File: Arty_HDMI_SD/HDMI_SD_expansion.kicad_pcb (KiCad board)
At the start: 2 copper layers, 13 parts, among them J1 0015912120, J2 SD_card_slot, J3 0015912120, J4 2000-1-2-41-00-BK

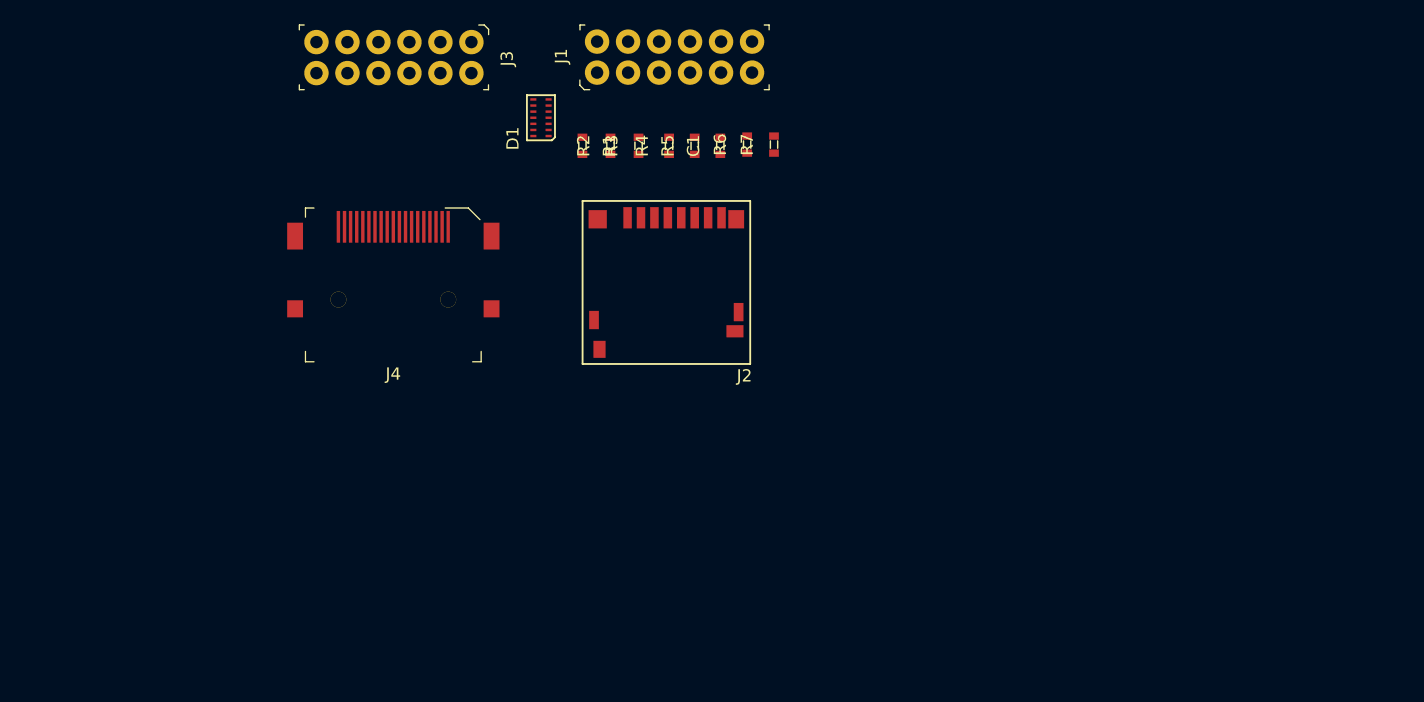
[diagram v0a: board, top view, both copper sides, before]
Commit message: Added USB SPI Interface
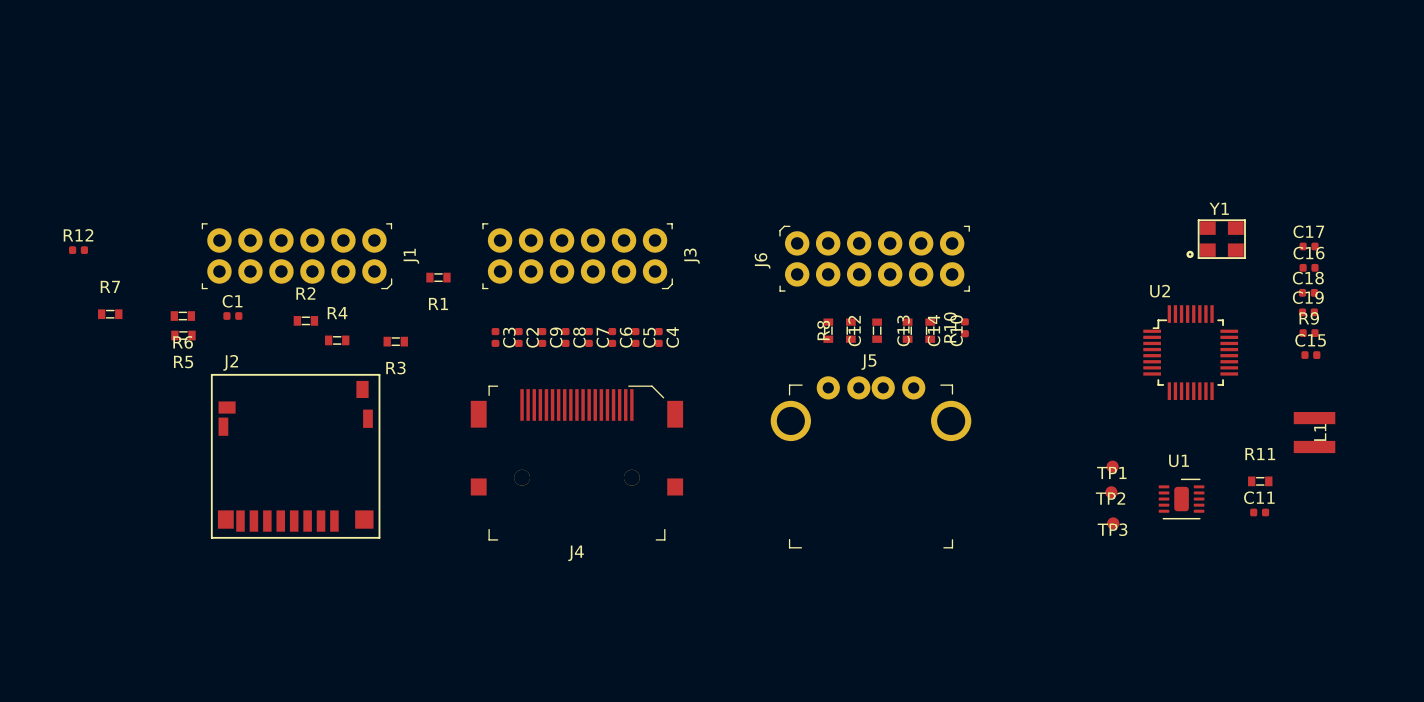
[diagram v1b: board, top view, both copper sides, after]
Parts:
- removed D1: TPD6E05U06, antmicro-footprints:TPD6E05U06
- added C10: C_22u_0603, antmicro-footprints:0603-cap, F.Cu at (164.2, 96.2)
- added C11: C_10n_0402, antmicro-footprints:0402-cap, F.Cu at (191.2, 111.0)
- added C12: C_22u_0603, antmicro-footprints:0603-cap, F.Cu at (155.8, 96.2)
- added C13: C_22u_0603, antmicro-footprints:0603-cap, F.Cu at (159.8, 96.2)
- added C14: C_22u_0603, antmicro-footprints:0603-cap, F.Cu at (162.3, 96.2)
- added C15: C_100n_0402_6V3, antmicro-footprints:0402-cap, F.Cu at (195.4, 98.2)
- added C16: C_22p_0402, antmicro-footprints:0402-cap, F.Cu at (195.2, 91.0)
- added C17: C_22p_0402, antmicro-footprints:0402-cap, F.Cu at (195.2, 89.2)
- added C18: C_100n_0402_6V3, antmicro-footprints:0402-cap, F.Cu at (195.2, 93.0)
- added C19: C_100n_0402_6V3, antmicro-footprints:0402-cap, F.Cu at (195.2, 94.7)
- added C2: C_100n_0402_6V3, antmicro-footprints:0402-cap, F.Cu at (130.5, 96.7)
- added C3: C_100n_0402_6V3, antmicro-footprints:0402-cap, F.Cu at (128.6, 96.7)
- added C4: C_100n_0402_6V3, antmicro-footprints:0402-cap, F.Cu at (142.0, 96.7)
- added C5: C_100n_0402_6V3, antmicro-footprints:0402-cap, F.Cu at (140.1, 96.7)
- added C6: C_100n_0402_6V3, antmicro-footprints:0402-cap, F.Cu at (138.1, 96.7)
- added C7: C_100n_0402_6V3, antmicro-footprints:0402-cap, F.Cu at (136.2, 96.7)
- added C8: C_100n_0402_6V3, antmicro-footprints:0402-cap, F.Cu at (134.3, 96.7)
- added C9: C_100n_0402_6V3, antmicro-footprints:0402-cap, F.Cu at (132.4, 96.7)
- added J5: UE27AC54100, antmicro-footprints:USB_A_Female_UE27AC54100, F.Cu at (159.3, 103.5)
- added J6: 0015912120, antmicro-footprints:PinHeader_6x2_P2.54mm_Horizontal_Mirrored, F.Cu at (153.3, 88.8)
- added L1: XFL4020-102MEB, antmicro-footprints:XFL4020-102MEB, F.Cu at (195.7, 104.5)
- added R10: R_22R_0402, antmicro-footprints:0402-res, F.Cu at (167.1, 95.9)
- added R11: R_0R_0603, antmicro-footprints:0603-res, F.Cu at (191.2, 108.5)
- added R12: R_220R_0402, antmicro-footprints:0402-res, F.Cu at (94.4, 89.5)
- added R8: R_0R_0603, antmicro-footprints:0603-res, F.Cu at (157.7, 96.2)
- added R9: R_22R_0402, antmicro-footprints:0402-res, F.Cu at (195.2, 96.3)
- added TP1: TP_SMD1MM, antmicro-footprints:Testpoint_smd_1mm, F.Cu at (179.2, 107.3)
- added TP2: TP_SMD1MM, antmicro-footprints:Testpoint_smd_1mm, F.Cu at (179.1, 109.5)
- added TP3: TP_SMD1MM, antmicro-footprints:Testpoint_smd_1mm, F.Cu at (179.2, 112.0)
- added U1: TPS61232DRCT, antmicro-footprints:VSON-10-1EP_3x3mm, F.Cu at (184.6, 110.2)
- added U2: MAX3421EEHJ, antmicro-footprints:TQFP-32_5x5mm, F.Cu at (185.6, 98.0)
- added Y1: KX-7_12,MHz, antmicro-footprints:KX-7, F.Cu at (188.1, 88.6)
- C1: value C_1u_0603 -> C_100n_0402_6V3; footprint antmicro-footprints:0603-cap -> antmicro-footprints:0402-cap
- J1, J3: footprint antmicro-footprints:PinHeader_6x2_P2.54mm_Horizontal -> antmicro-footprints:PinHeader_6x2_P2.54mm_Horizontal_Mirrored
- J2: value SD_card_slot -> 1140084168; footprint antmicro-footprints:1140084168 -> antmicro-footprints:MicroSD_1140084168
- R1, R2, R3, R4, R5, R6, R7: value R_10k_0603 -> R_20k_0603
- moved R7 56.1 mm to (97.0, 94.8), turned to 0 degrees
- moved R6 48.3 mm to (103.0, 95.0), turned to 180 degrees
- moved R5 44.7 mm to (103.0, 96.5), turned to 180 degrees
- moved C1 42.3 mm to (107.0, 95.0), turned to 0 degrees
- moved J2 40.0 mm to (112.2, 106.5), turned to 0 degrees
- moved R4 31.5 mm to (115.6, 97.0), turned to 0 degrees
- moved R2 28.8 mm to (113.0, 95.3), turned to 0 degrees
- moved R3 25.6 mm to (120.4, 97.0), turned to 180 degrees
- moved J1 24.6 mm to (118.7, 91.5), turned to 270 degrees
- moved J3 24.2 mm to (141.7, 91.5)
- moved J4 21.0 mm to (135.2, 106.7)
- moved R1 16.0 mm to (123.9, 91.8), turned to 180 degrees
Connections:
- J1 pad 1: /SS -> /CD_DAT3
- J1 pad 11: +5V -> +3V3
- J1 pad 12: +5V -> +3V3
- J1 pad 2: /MOSI -> /DAT1
- J1 pad 3: /MOSI -> /MOSI_CMD
- J1 pad 4: /SCK -> /DAT2
- J1 pad 5: /MISO -> /MISO_DAT0
- J1 pad 6: /TDMS_D1_P -> /CD
- J1 pad 8: /TDMS_D1_N -> /NC_EN
- J2 pad 10: /CD2 -> GND
- J2 pad 2: /SS -> /CD_DAT3
- J2 pad 3: /MOSI -> /MOSI_CMD
- J2 pad 7: /MISO -> /MISO_DAT0
- J2 pad 9: /CD -> Net-(J2-Pad9)
- J2 pad ~: (no net) -> GND
- J3 pad 11: +5V -> +3V3
- J3 pad 12: +5V -> +3V3
- J4 pad 1: /TDMS_D2_P -> /C_TDMS_D2_P
- J4 pad 10: /TDMS_CLK_N -> /C_TDMS_CLK_P
- J4 pad 12: /TDMS_CLK_P -> /C_TDMS_CLK_N
- J4 pad 18: +5V -> /NC
- J4 pad 3: /TDMS_D2_N -> /C_TDMS_D2_N
- J4 pad 4: /TDMS_D1_P -> /C_TDMS_D1_P
- J4 pad 6: /TDMS_D1_N -> /C_TDMS_D1_N
- J4 pad 7: /TDMS_D0_P -> /C_TDMS_D0_P
- J4 pad 9: /TDMS_D0_N -> /C_TDMS_D0_N
- R1 pad 2: /DAT2 -> /CD
- R2 pad 2: /SS -> /DAT1
- R3 pad 2: /MOSI -> /MISO_DAT0
- R5 pad 2: /MISO -> /MOSI_CMD
- R6 pad 2: /DAT1 -> /CD_DAT3
- R7 pad 2: /CD -> /DAT2

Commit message: Schematic updates
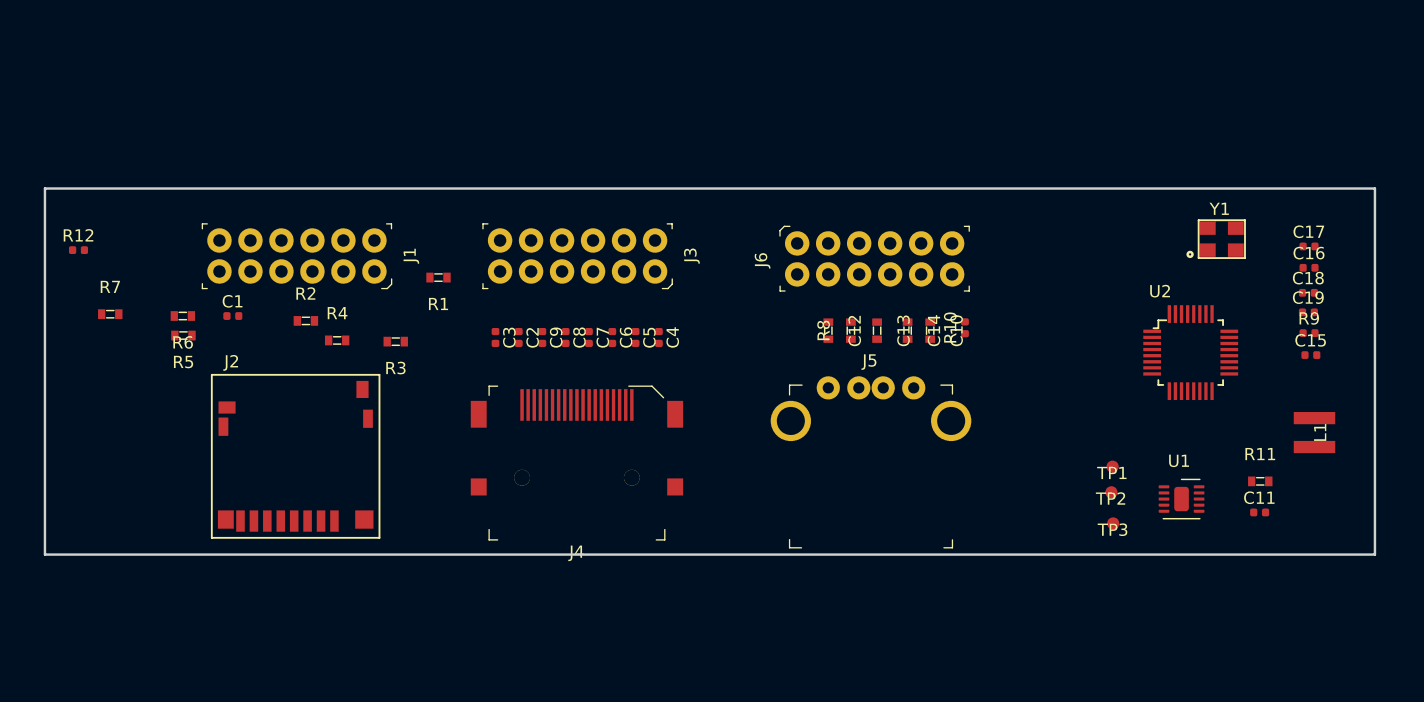
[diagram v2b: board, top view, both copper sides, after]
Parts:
- R11: value R_0R_0603 -> R_10k_0603
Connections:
- J5 pad 1: GND -> Net-(C15-Pad1)
- J5 pad 2: Net-(D1-Pad2) -> Net-(J5-Pad2)
- J5 pad 3: Net-(J5-Pad3) -> Net-(D1-Pad2)
- J5 pad 4: Net-(C15-Pad1) -> GND
- J5 pad SH: GND -> Net-(J5-PadSH)
- J6 pad 2: Net-(J6-Pad2) -> /GPX_USB
- J6 pad 4: Net-(J6-Pad4) -> /RST_USB
- R9 pad 1: Net-(J5-Pad3) -> Net-(J5-Pad2)
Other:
- board outline added: 109 x 30 mm

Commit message: Added testpads
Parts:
- added TP10: TP_SMD1MM, antmicro-footprints:Testpoint_smd_1mm, F.Cu at (173.9, 112.5)
- added TP4: TP_SMD1MM, antmicro-footprints:Testpoint_smd_1mm, F.Cu at (179.0, 105.0)
- added TP5: TP_SMD1MM, antmicro-footprints:Testpoint_smd_1mm, F.Cu at (183.0, 104.2)
- added TP6: TP_SMD1MM, antmicro-footprints:Testpoint_smd_1mm, F.Cu at (185.9, 104.1)
- added TP7: TP_SMD1MM, antmicro-footprints:Testpoint_smd_1mm, F.Cu at (179.4, 101.6)
- added TP8: TP_SMD1MM, antmicro-footprints:Testpoint_smd_1mm, F.Cu at (173.8, 110.5)
- added TP9: TP_SMD1MM, antmicro-footprints:Testpoint_smd_1mm, F.Cu at (173.7, 104.5)
- moved J6 11.6 mm to (164.7, 91.3), turned to 270 degrees
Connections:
- J6 pad 6: Net-(J6-Pad6) -> /INT_USB
- R11 pad 2: Net-(R11-Pad2) -> /INT_USB
- U2 pad 18: Net-(R11-Pad2) -> /INT_USB

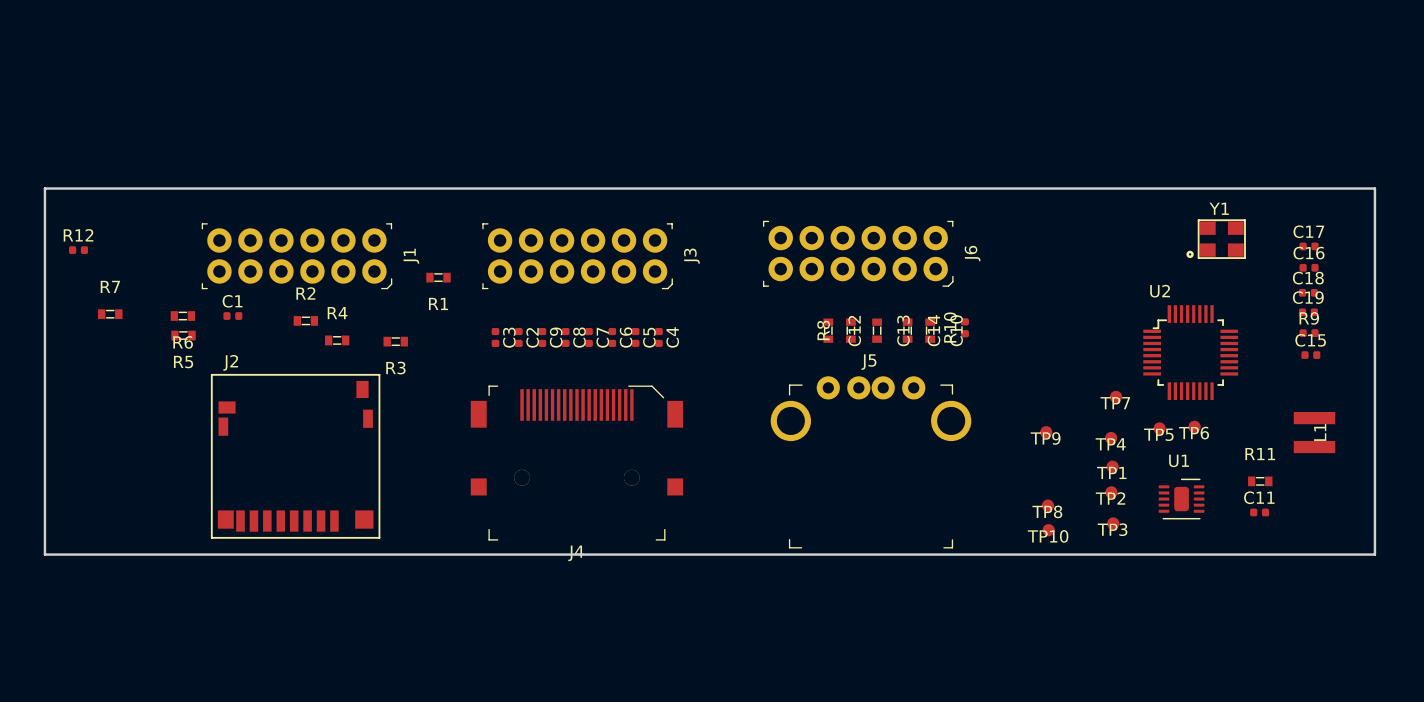
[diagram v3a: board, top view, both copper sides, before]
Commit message: Optimized component placement
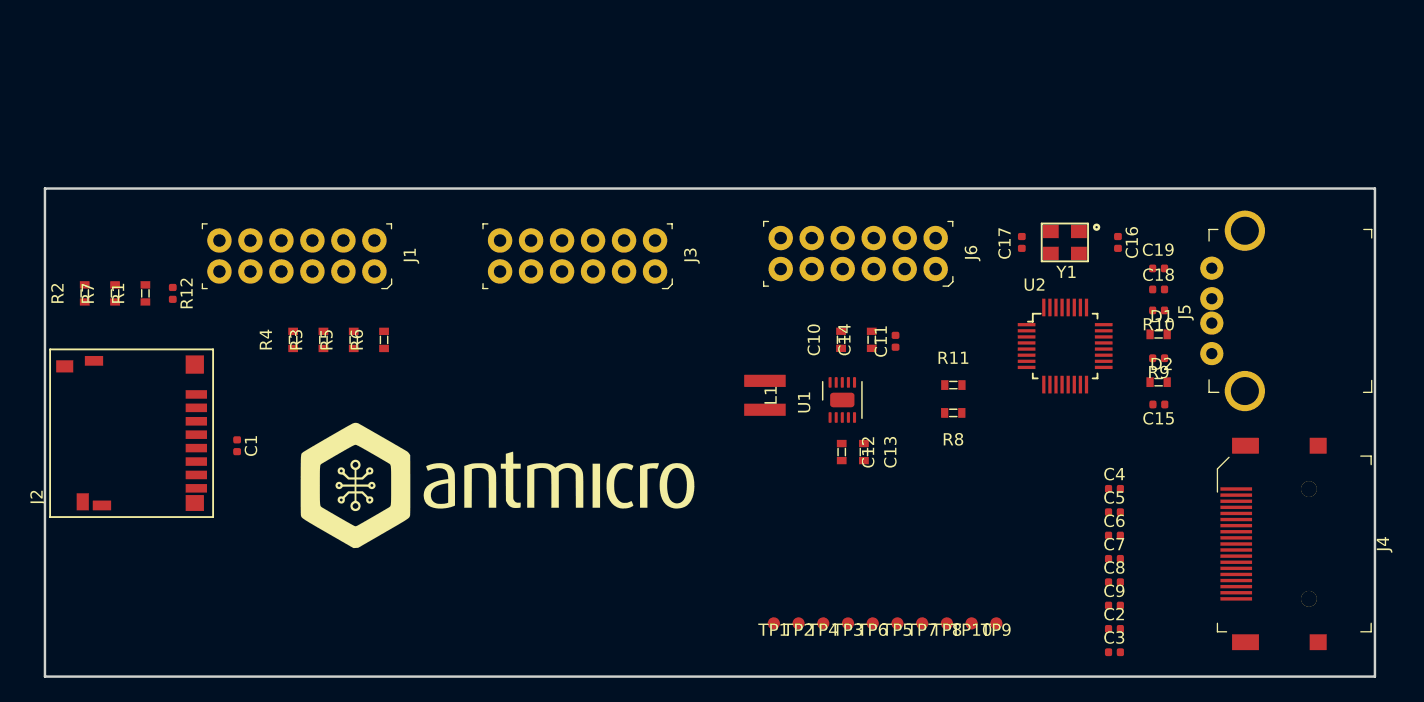
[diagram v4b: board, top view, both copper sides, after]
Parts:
- added D1: PGB1010603MR, antmicro-footprints:PGB1010603MR, F.Cu at (182.9, 96.5)
- added D2: PGB1010603MR, antmicro-footprints:PGB1010603MR, F.Cu at (182.9, 100.4)
- added G***: LOGO, antmicro-footprints:antmicro-logo_scaled, F.Cu at (128.7, 109.1)
- moved J4 58.9 mm to (193.7, 113.6), turned to 270 degrees
- moved C3 56.9 mm to (179.3, 122.5), turned to 0 degrees
- moved C2 54.3 mm to (179.3, 120.6), turned to 0 degrees
- moved C9 51.8 mm to (179.3, 118.7), turned to 0 degrees
- moved C8 49.2 mm to (179.3, 116.8), turned to 0 degrees
- moved C7 46.7 mm to (179.3, 114.9), turned to 0 degrees
- moved L1 45.1 mm to (150.7, 101.5)
- moved C6 44.2 mm to (179.3, 112.9), turned to 0 degrees
- moved C5 41.8 mm to (179.3, 111.0), turned to 0 degrees
- moved C4 39.3 mm to (179.3, 109.1), turned to 0 degrees
- moved C11 33.0 mm to (161.4, 97.0), turned to 90 degrees
- moved J5 31.9 mm to (190.0, 94.5), turned to 90 degrees
- moved TP6 30.9 mm to (159.5, 120.2)
- moved TP1 30.6 mm to (151.4, 120.2)
- moved U1 28.6 mm to (157.2, 102.0), turned to 90 degrees
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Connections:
- C15 pad 1: Net-(C15-Pad1) -> +5V
- J5 pad 1: Net-(C15-Pad1) -> +5V
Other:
- board size 109 x 30 mm -> 109 x 40 mm

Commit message: Added logotype, rotated SD card
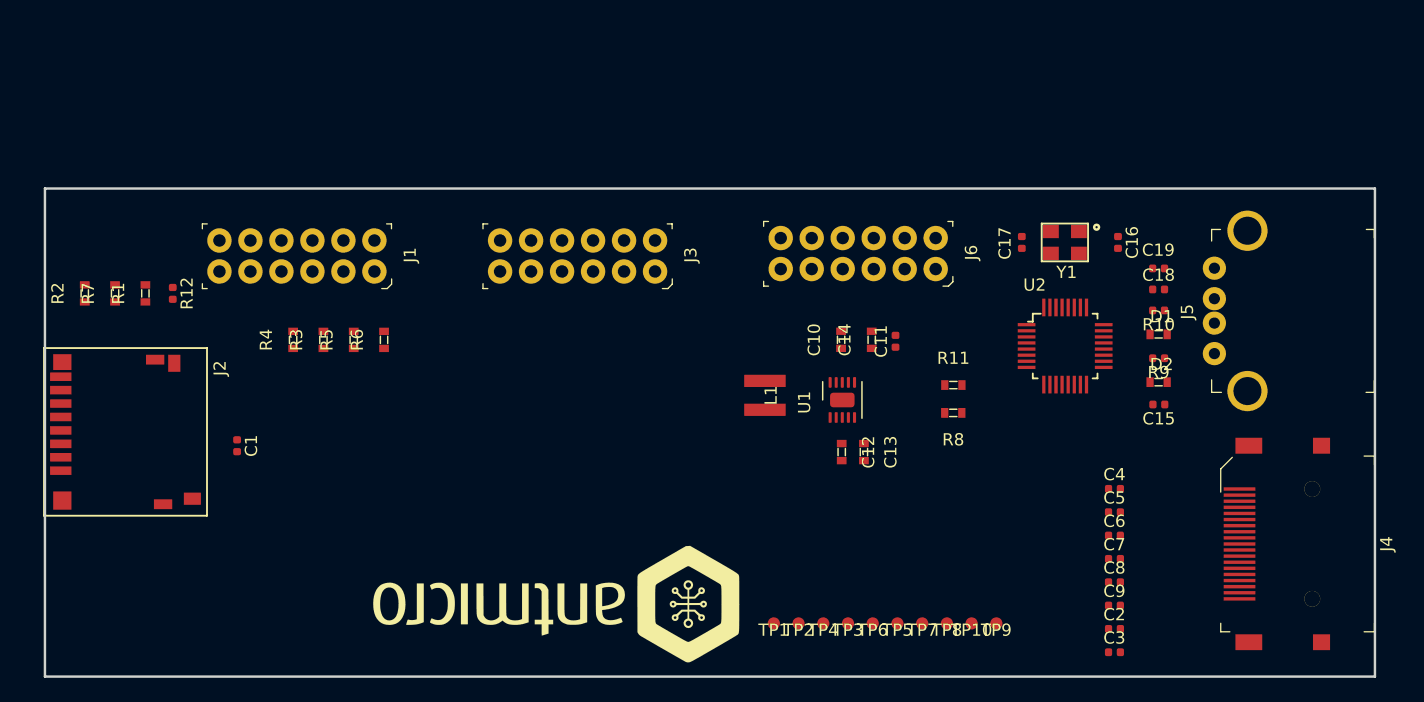
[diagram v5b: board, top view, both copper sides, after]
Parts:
- removed the G*** at (128.7, 109.1)
- added G***: LOGO, antmicro-footprints:antmicro-logo_scaled_30mm, F.Cu at (133.6, 118.3)
- moved J2 0.50 mm to (98.2, 104.5), turned to 270 degrees
- moved J4 0.27 mm to (194.0, 113.6)
- moved J5 0.21 mm to (190.2, 94.5)
